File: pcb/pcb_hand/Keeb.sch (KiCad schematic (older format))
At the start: 68 parts, among them K00 KEYSW, K01 KEYSW, K02 KEYSW, K03 KEYSW, K04 KEYSW, K05 KEYSW, K10 KEYSW, K11 KEYSW, K12 KEYSW, K13 KEYSW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

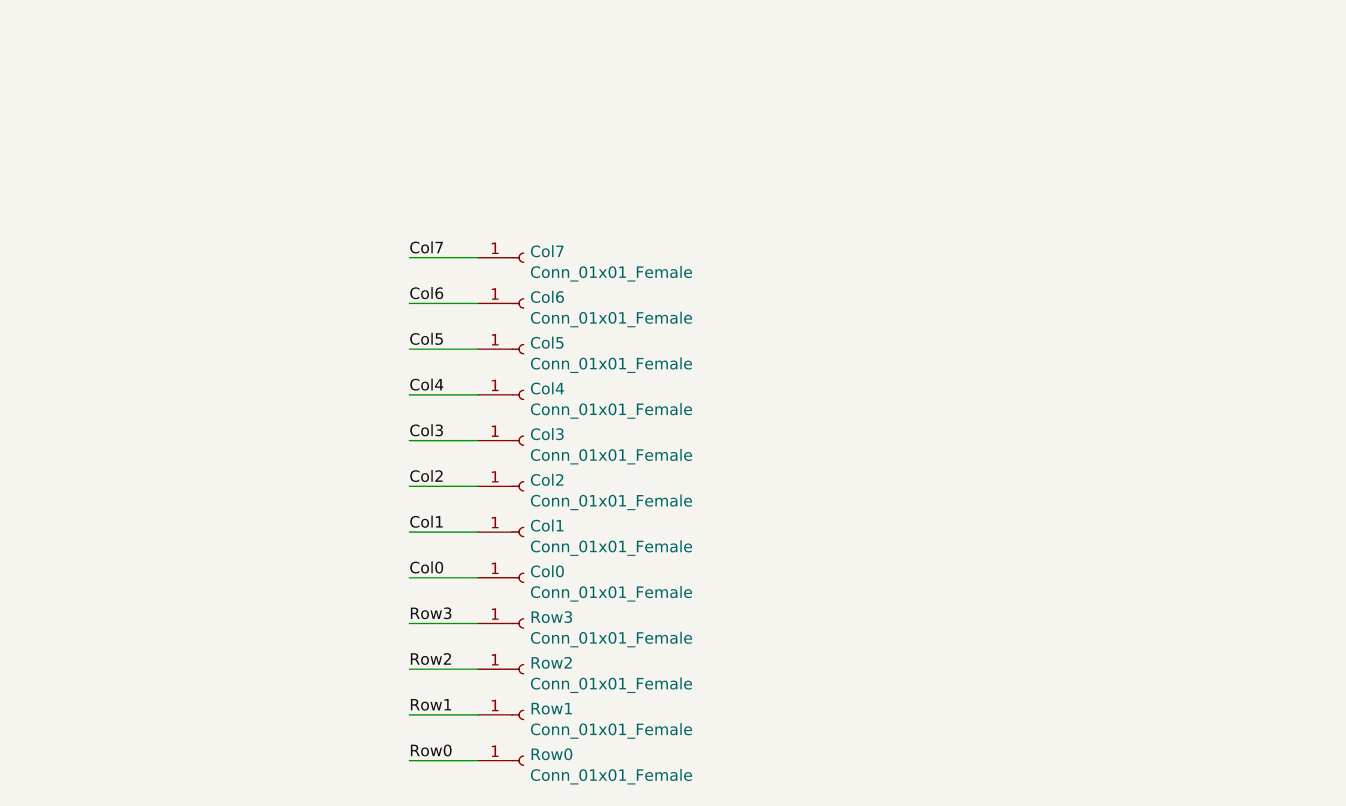
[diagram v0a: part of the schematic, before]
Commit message: Updated layout to use hirose connectors
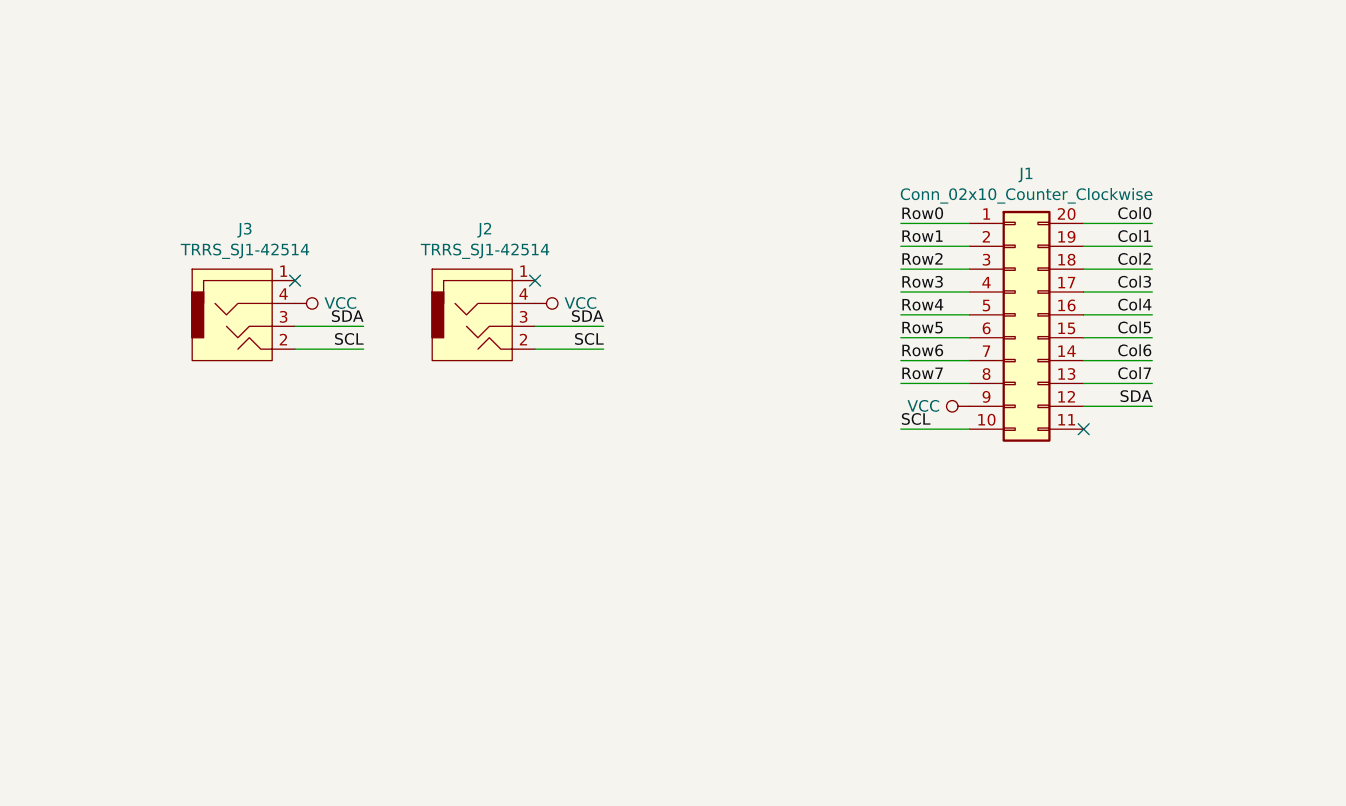
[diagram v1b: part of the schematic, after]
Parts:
- removed Col0, Col1, Col2, Col3, Col4, Col5, Col6, Col7, Row0, Row1, Row2, Row3: Conn_01x01_Female, SVastaCustomParts:Mill-Max_Pin_Socket_7305-0-15-15-47-27-10-0, symbol Connector:Conn_01x01_Female
- added J1: Conn_02x10_Counter_Clockwise, SVastaCustomParts:Backplane_Connector_Hirose_PCN_20pos_Receptacle, symbol Connector_Generic:Conn_02x10_Counter_Clockwise
- added J2, J3: TRRS_SJ1-42514, SVastaCustomParts:3.5mm_Cut_out, symbol SVastaCustomParts:TRRS_SJ1-42514
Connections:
- net Col0: now also J1.20 (Pin_20)
- net Col1: now also J1.19 (Pin_19)
- net Col2: now also J1.18 (Pin_18)
- net Col3: now also J1.17 (Pin_17)
- net Col4: now also J1.16 (Pin_16)
- net Col5: now also J1.15 (Pin_15)
- net Col6: now also J1.14 (Pin_14)
- net Col7: now also J1.13 (Pin_13)
- net Row0: now also J1.1 (Pin_1)
- net Row1: now also J1.2 (Pin_2)
- net Row2: now also J1.3 (Pin_3)
- net Row3: now also J1.4 (Pin_4)
- new net Row4: J1.5 (Pin_5)
- new net Row5: J1.6 (Pin_6)
- new net Row6: J1.7 (Pin_7)
- new net Row7: J1.8 (Pin_8)
- new net SCL: J1.10 (Pin_10), J2.2, J3.2
- new net SDA: J1.12 (Pin_12), J2.3, J3.3
- new net VCC: J1.9 (Pin_9), J2.4, J3.4
- no-connect marks 0 -> 3
